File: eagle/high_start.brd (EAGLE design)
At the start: 100.8 x 80.8 mm, 32 parts, among them Q1 16Mhz, Q2 IRF510, Q3 IRF510, Q4 IRF510, U2 ATMEGA328P_PDIP, X1 22-23-2041, X2 22-23-2041, X3 22-23-2041, X4 22-23-2041

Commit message: tied led cathodes to gnd
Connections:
- net GND: now also LED1.K, LED2.K, LED3.K
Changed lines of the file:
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@@
 <contactref element="IGN3" pad="1"/>
 <contactref element="IGN2" pad="1"/>
+<contactref element="LED1" pad="K"/>
+<contactref element="LED3" pad="K"/>
+<contactref element="LED2" pad="K"/>
 <wire x1="-68.58" y1="-190.5" x2="-68.58" y2="-175.26" width="0" layer="19" extent="1-1"/>
 <wire x1="-68.58" y1="-205.74" x2="-68.58" y2="-190.5" width="0" layer="19" extent="1-1"/>
@@
 <wire x1="-73.66" y1="-279.4" x2="-73.66" y2="-264.16" width="0" layer="19" extent="1-1"/>
 <wire x1="-73.66" y1="-294.64" x2="-73.66" y2="-279.4" width="0" layer="19" extent="1-1"/>
+<wire x1="-72.39" y1="-309.88" x2="-73.66" y2="-294.64" width="0" layer="19" extent="1-1"/>
+<wire x1="-72.39" y1="-323.85" x2="-72.39" y2="-309.88" width="0" layer="19" extent="1-1"/>
+<wire x1="-72.39" y1="-337.82" x2="-72.39" y2="-323.85" width="0" layer="19" extent="1-1"/>
 <wire x1="-24.13" y1="-86.36" x2="-68.58" y2="-175.26" width="0" layer="19" extent="1-1"/>
 <wire x1="-24.13" y1="-71.12" x2="-24.13" y2="-86.36" width="0" layer="19" extent="1-1"/>

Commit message: added battery and reg and layed out board
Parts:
- removed GPS_SPI: 22-23-2021, con-molex:22-23-2021
- removed X1, X2, X3, X4: 22-23-2041, con-molex:22-23-2041
- added BATTERY: 22-23-2021, con-molex:22-23-2021
- added C4: 22u, rcl:B45181A
- added GPS, I2C_1, I2C_2, I2C_3: 22-23-2041, con-molex:22-23-2041
- added IC1: 7805L, linear:TO92
- moved LED3 408.3 mm to (91.4, 35.6), turned to 270 degrees
- moved LED2 384.0 mm to (91.4, 22.9), turned to 270 degrees
- moved IGN3 362.9 mm to (91.4, 29.2), turned to 270 degrees
- moved LED1 360.1 mm to (91.4, 10.2), turned to 270 degrees
- moved IGN2 338.2 mm to (91.4, 16.5), turned to 270 degrees
- moved R4 322.9 mm to (86.4, 33.0), turned to 270 degrees
- moved IGN1 314.1 mm to (91.4, 3.81), turned to 270 degrees
- moved R3 299.9 mm to (86.4, 20.3), turned to 270 degrees
- moved R2 277.6 mm to (86.4, 7.62), turned to 270 degrees
- moved SERVO3 245.5 mm to (54.6, 5.08), turned to 180 degrees
- moved SERVO2 237.9 mm to (54.6, 11.4), turned to 180 degrees
- moved Q4 222.0 mm to (69.8, 33.0), turned to 270 degrees
- moved D3 220.9 mm to (26.7, 38.1), turned to 270 degrees
- moved SERVO1 210.8 mm to (19.1, 15.2), turned to 270 degrees
- moved D2 183.5 mm to (29.2, 38.1), turned to 270 degrees
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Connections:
- net +5V: now also C4.+, GPS.4, I2C_1.4, I2C_2.4, I2C_3.4, IC1.1; no longer X1.4, X2.4, X3.4, X4.4
- net +9V: now also BATTERY.2, IC1.3
- net GND: now also BATTERY.1, C4.-, GPS.3, I2C_1.3, I2C_2.3, I2C_3.3, IC1.2; no longer X1.3, X2.3, X3.3, X4.3
- net N$1: now also I2C_1.2, I2C_2.2, I2C_3.2; no longer X1.2, X2.2, X3.2, X4.2
- net N$2: now also I2C_1.1, I2C_2.1, I2C_3.1; no longer X1.1, X2.1, X3.1, X4.1
- net N$3: now also GPS.1; no longer GPS_SPI.2
- net N$6: now also GPS.2; no longer GPS_SPI.1
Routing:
- net GND: track 123.6 -> 0.00 mm
- net +5V: track 33.9 -> 0.00 mm
- net N$5: track 15.2 -> 0.00 mm
- net N$43: track 14.6 -> 0.00 mm
- net N$4: track 14.3 -> 0.00 mm
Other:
- board size 100.8 x 80.8 mm -> 100.1 x 80 mm

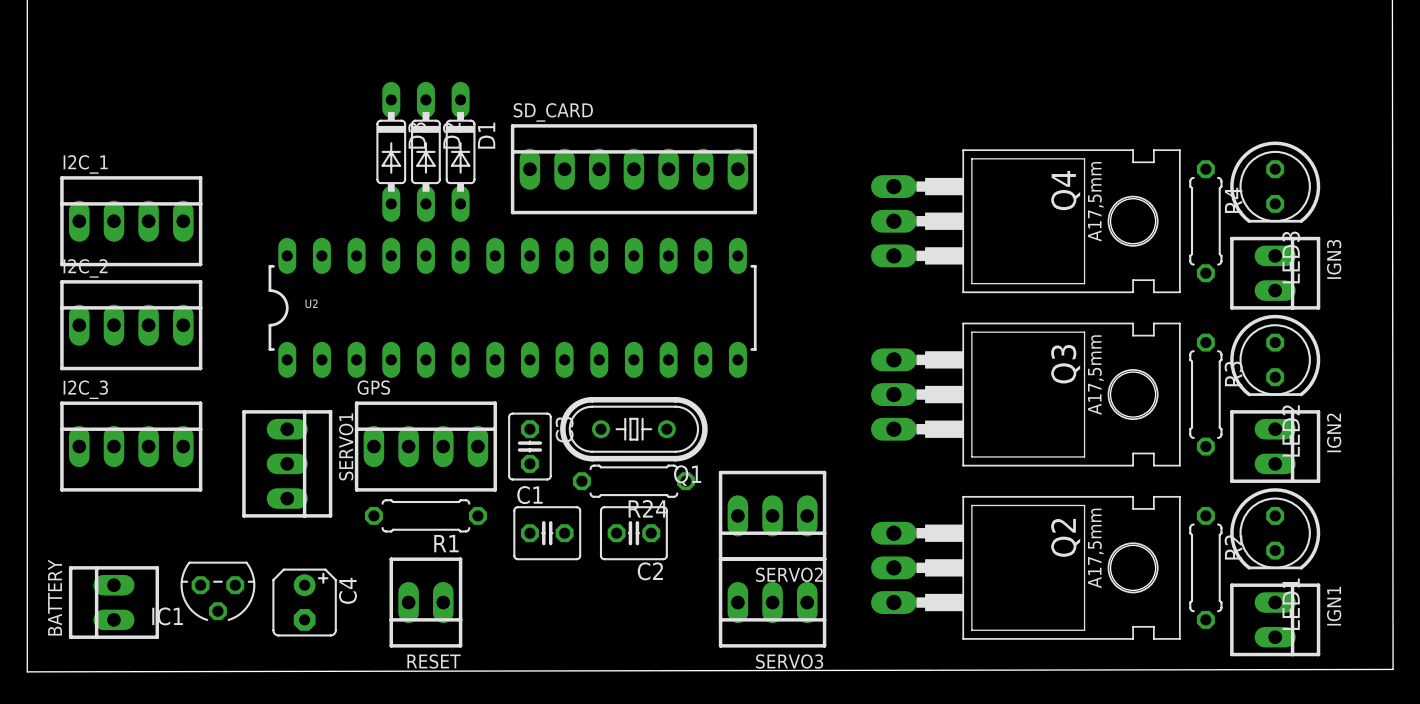
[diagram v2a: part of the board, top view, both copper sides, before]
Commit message: moved power connector between fets and micro
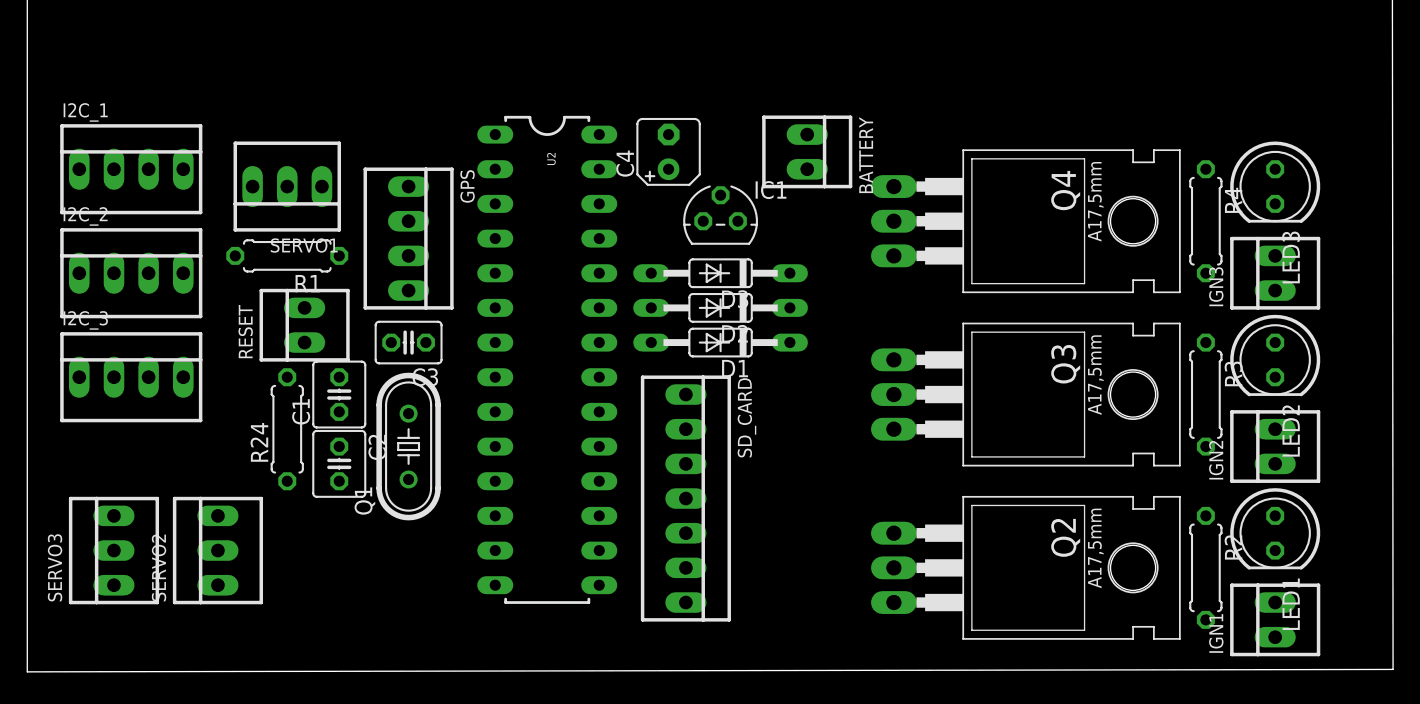
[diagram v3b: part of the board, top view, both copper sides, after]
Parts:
- D1, D2, D3: value 1N4148DO35-7 -> 1N4148DO35-10; device diode:DO35-7 -> diode:DO35-10
- moved BATTERY 60.6 mm to (57.1, 38.1), turned to 270 degrees
- moved SERVO3 48.4 mm to (6.35, 8.89), turned to 90 degrees
- moved IC1 45.5 mm to (50.8, 33.0), turned to 0 degrees
- moved C4 42.4 mm to (47.0, 38.1), turned to 90 degrees
- moved SERVO2 40.7 mm to (14.0, 8.89), turned to 90 degrees
- moved D3 25.7 mm to (50.8, 29.2), turned to 180 degrees
- moved R24 25.7 mm to (19.1, 17.8), turned to 90 degrees
- moved SD_CARD 24.4 mm to (48.3, 12.7), turned to 270 degrees
- moved D2 24.4 mm to (50.8, 26.7), turned to 180 degrees
- moved D1 23.6 mm to (50.8, 24.1), turned to 180 degrees
- moved C2 22.2 mm to (22.9, 15.2), turned to 270 degrees
- moved RESET 22.2 mm to (20.3, 25.4), turned to 90 degrees
- moved R1 21.6 mm to (19.1, 30.5)
- moved SERVO1 20.3 mm to (19.1, 35.6), turned to 180 degrees
- moved C1 18.3 mm to (22.9, 20.3), turned to 90 degrees
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
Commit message: routed
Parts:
- moved SERVO1 21.6 mm to (8.89, 16.5)
- moved I2C_3 5.08 mm to (7.62, 26.7), turned to 180 degrees
- moved I2C_2 3.81 mm to (7.62, 33.0), turned to 180 degrees
- moved R1 3.30 mm to (22.4, 30.5), turned to 90 degrees
- moved I2C_1 2.54 mm to (7.62, 39.4), turned to 180 degrees
- moved RESET 2.54 mm to (17.8, 25.4), turned to 180 degrees
- moved SD_CARD 1.27 mm to (49.5, 12.7)
- moved C4 0.51 mm to (47.5, 38.1)
- turned LED1 to 0 degrees
- turned LED2 to 0 degrees
- turned LED3 to 0 degrees
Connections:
- net +5V: now also U2.21
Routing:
- net GND: track 0.00 -> 254.5 mm, vias 0 -> 4
- net +5V: track 0.00 -> 184.5 mm, vias 0 -> 2
- net +9V: track 0.00 -> 65.2 mm
- net N$15: track 0.00 -> 53.9 mm
- net N$1: track 0.00 -> 49.9 mm
- net N$2: track 0.00 -> 47.8 mm
- net N$7: track 0.00 -> 40.3 mm
- net N$8: track 0.00 -> 34.8 mm
- net N$17: track 0.00 -> 31.6 mm
- net N$24: track 0.00 -> 28.8 mm
- net N$25: track 0.00 -> 28.8 mm
- net N$26: track 0.00 -> 28.2 mm
- net N$43: track 0.00 -> 25.5 mm
- net N$16: track 0.00 -> 23.5 mm
- net N$4: track 0.00 -> 16.7 mm
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
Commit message: milling on board
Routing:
- net N$24: track 28.8 -> 30.4 mm
- net N$17: track 31.6 -> 32.6 mm
- net N$16: track 23.5 -> 24.4 mm
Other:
- board size 100.1 x 80 mm -> 100.1 x 80.8 mm
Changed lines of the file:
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@@
 <wire x1="100" y1="80" x2="0" y2="80" width="0" layer="20"/>
 <wire x1="0" y1="80" x2="0" y2="0" width="0" layer="20"/>
+<wire x1="15.748" y1="39.37" x2="17.526" y2="39.37" width="1.6764" layer="46"/>
+<wire x1="17.526" y1="39.37" x2="17.526" y2="37.592" width="1.6764" layer="46"/>
+<wire x1="17.526" y1="37.592" x2="15.748" y2="37.592" width="1.6764" layer="46"/>
+<wire x1="15.748" y1="37.592" x2="15.748" y2="39.37" width="1.6764" layer="46"/>
+<wire x1="21.844" y1="6.35" x2="29.972" y2="6.35" width="1.6764" layer="46"/>
+<wire x1="29.972" y1="6.35" x2="29.972" y2="4.572" width="1.6764" layer="46"/>
+<wire x1="29.972" y1="4.572" x2="21.844" y2="4.572" width="1.6764" layer="46"/>
+<wire x1="21.844" y1="4.572" x2="21.844" y2="6.35" width="1.6764" layer="46"/>
+<wire x1="69.342" y1="35.052" x2="83.312" y2="35.052" width="1.6764" layer="46"/>
+<wire x1="83.312" y1="35.052" x2="83.312" y2="33.274" width="1.6764" layer="46"/>
+<wire x1="83.312" y1="33.274" x2="69.342" y2="33.274" width="1.6764" layer="46"/>
+<wire x1="69.342" y1="33.274" x2="69.342" y2="35.052" width="1.6764" layer="46"/>
+<wire x1="69.342" y1="8.382" x2="83.312" y2="8.382" width="1.6764" layer="46"/>
+<wire x1="83.312" y1="8.382" x2="83.312" y2="6.604" width="1.6764" layer="46"/>
+<wire x1="83.312" y1="6.604" x2="69.342" y2="6.604" width="1.6764" layer="46"/>
+<wire x1="69.342" y1="6.604" x2="69.342" y2="8.382" width="1.6764" layer="46"/>
+<wire x1="1.27" y1="44.45" x2="1.27" y2="0.508" width="1.6764" layer="46"/>
+<wire x1="1.27" y1="0.508" x2="2.54" y2="-0.762" width="1.6764" layer="46"/>
+<wire x1="2.54" y1="-0.762" x2="93.98" y2="-0.762" width="1.6764" layer="46"/>
+<wire x1="93.98" y1="-0.762" x2="96.266" y2="1.778" width="1.6764" layer="46"/>
+<wire x1="96.266" y1="1.778" x2="96.266" y2="39.37" width="1.6764" layer="46"/>
+<wire x1="96.266" y1="39.37" x2="92.202" y2="41.91" width="1.6764" layer="46"/>
+<wire x1="92.202" y1="41.91" x2="43.18" y2="41.91" width="1.6764" layer="46"/>
+<wire x1="43.18" y1="41.91" x2="38.354" y2="45.72" width="1.6764" layer="46"/>
+<wire x1="38.354" y1="45.72" x2="2.54" y2="45.72" width="1.6764" layer="46"/>
+<wire x1="1.27" y1="44.45" x2="2.54" y2="45.72" width="1.6764" layer="46"/>
+<wire x1="69.342" y1="27.686" x2="69.342" y2="20.32" width="1.6764" layer="46"/>
+<wire x1="69.342" y1="20.32" x2="83.312" y2="20.32" width="1.6764" layer="46"/>
+<wire x1="83.312" y1="20.32" x2="83.312" y2="27.686" width="1.6764" layer="46"/>
+<wire x1="83.312" y1="27.686" x2="69.342" y2="27.686" width="1.6764" layer="46"/>
 </plain>
 <attributes>
@@
 <contactref element="SERVO2" pad="1"/>
 <wire x1="31.0642" y1="13.4366" x2="33.8836" y2="13.4366" width="0.7112" layer="16"/>
-<wire x1="24.0538" y1="6.4262" x2="31.0642" y2="13.4366" width="0.7112" layer="16"/>
-<wire x1="14.0208" y1="6.4262" x2="24.0538" y2="6.4262" width="0.7112" layer="16"/>
+<wire x1="15.9258" y1="6.4262" x2="17.78" y2="10.16" width="0.7112" layer="16"/>
+<wire x1="17.78" y1="10.16" x2="19.05" y2="11.43" width="0.7112" layer="16"/>
+<wire x1="19.05" y1="11.43" x2="29.21" y2="11.43" width="0.7112" layer="16"/>
+<wire x1="29.21" y1="11.43" x2="31.0642" y2="13.2842" width="0.7112" layer="16"/>
+<wire x1="31.0642" y1="13.2842" x2="31.0642" y2="13.4366" width="0.7112" layer="16"/>
+<wire x1="14.0208" y1="6.4262" x2="15.9258" y2="6.4262" width="0.7112" layer="16"/>
 <wire x1="33.8836" y1="13.4366" x2="34.29" y2="13.97" width="0.7112" layer="16"/>
 <wire x1="14.0208" y1="6.4262" x2="13.97" y2="6.35" width="0.7112" layer="16"/>
@@
 <contactref element="SERVO3" pad="1"/>
 <contactref element="U2" pad="12"/>
-<wire x1="31.242" y1="11.0998" x2="33.8836" y2="11.0998" width="0.7112" layer="16"/>
-<wire x1="24.8158" y1="4.6736" x2="31.242" y2="11.0998" width="0.7112" layer="16"/>
-<wire x1="7.5946" y1="4.6736" x2="24.8158" y2="4.6736" width="0.7112" layer="16"/>
+<wire x1="31.496" y1="11.0998" x2="33.8836" y2="11.0998" width="0.7112" layer="16"/>
+<wire x1="17.1958" y1="4.6736" x2="19.812" y2="9.906" width="0.7112" layer="16"/>
+<wire x1="19.812" y1="9.906" x2="29.718" y2="9.906" width="0.7112" layer="16"/>
+<wire x1="29.718" y1="9.906" x2="31.242" y2="10.922" width="0.7112" layer="16"/>
+<wire x1="31.242" y1="10.922" x2="31.496" y2="11.0998" width="0.7112" layer="16"/>
+<wire x1="7.5946" y1="4.6736" x2="17.1958" y2="4.6736" width="0.7112" layer="16"/>
 <wire x1="6.4262" y1="5.842" x2="7.5946" y2="4.6736" width="0.7112" layer="16"/>
 <wire x1="33.8836" y1="11.0998" x2="34.29" y2="11.43" width="0.7112" layer="16"/>
@@
 <contactref element="R2" pad="1"/>
 <contactref element="LED1" pad="A"/>
-<wire x1="87.3252" y1="11.684" x2="86.4616" y2="11.684" width="0.7112" layer="16"/>
+<wire x1="86.8172" y1="11.43" x2="86.4616" y2="11.684" width="0.7112" layer="16"/>
 <wire x1="86.4616" y1="11.684" x2="86.36" y2="11.43" width="0.7112" layer="16"/>
-<wire x1="87.3252" y1="11.684" x2="90.17" y2="10.16" width="0.7112" layer="16"/>
+<wire x1="86.8172" y1="11.43" x2="90.17" y2="10.16" width="0.7112" layer="16"/>
 </signal>
 <signal name="N$22">
 <contactref element="R3" pad="1"/>
 <contactref element="LED2" pad="A"/>
-<wire x1="87.3252" y1="24.5364" x2="86.4616" y2="24.5364" width="0.7112" layer="16"/>
-<wire x1="86.4616" y1="24.5364" x2="86.36" y2="24.13" width="0.7112" layer="16"/>
-<wire x1="87.3252" y1="24.5364" x2="90.17" y2="22.86" width="0.7112" layer="16"/>
+<wire x1="87.3252" y1="23.7744" x2="86.4616" y2="23.7744" width="0.7112" layer="16"/>
+<wire x1="86.4616" y1="23.7744" x2="86.36" y2="24.13" width="0.7112" layer="16"/>
+<wire x1="87.3252" y1="23.7744" x2="90.17" y2="22.86" width="0.7112" layer="16"/>
 </signal>
 <signal name="N$23">
@@
 <wire x1="86.4616" y1="4.0894" x2="86.36" y2="3.81" width="0.7112" layer="16"/>
 <wire x1="91.1352" y1="5.2578" x2="91.44" y2="5.08" width="0.7112" layer="16"/>
-<wire x1="77.1144" y1="4.6736" x2="63.6778" y2="4.6736" width="1.016" layer="16"/>
-<wire x1="85.217" y1="4.191" x2="77.1144" y2="4.6736" width="1.016" layer="16"/>
-<wire x1="85.2932" y1="4.191" x2="85.217" y2="4.191" width="1.016" layer="16"/>
-<wire x1="86.3854" y1="3.7592" x2="85.2932" y2="4.191" width="1.016" layer="16"/>
+<wire x1="63.3984" y1="4.6736" x2="63.6778" y2="4.6736" width="1.016" layer="16"/>
+<wire x1="68.199" y1="2.413" x2="63.3984" y2="4.6736" width="1.016" layer="16"/>
+<wire x1="85.2932" y1="2.413" x2="68.199" y2="2.413" width="1.016" layer="16"/>
+<wire x1="86.3854" y1="3.7592" x2="85.2932" y2="2.413" width="1.016" layer="16"/>
 <wire x1="63.6778" y1="4.6736" x2="63.5" y2="5.08" width="0.7112" layer="16"/>
 <wire x1="86.3854" y1="3.7592" x2="86.36" y2="3.81" width="0.7112" layer="16"/>
@@
 <wire x1="86.4616" y1="16.9418" x2="86.36" y2="16.51" width="0.7112" layer="16"/>
 <wire x1="91.1352" y1="17.526" x2="91.44" y2="17.78" width="0.7112" layer="16"/>
-<wire x1="77.1144" y1="17.526" x2="63.6778" y2="17.526" width="1.016" layer="16"/>
-<wire x1="85.217" y1="17.0434" x2="77.1144" y2="17.526" width="1.016" layer="16"/>
+<wire x1="83.4644" y1="17.526" x2="63.6778" y2="17.526" width="1.016" layer="16"/>
+<wire x1="85.217" y1="17.0434" x2="83.4644" y2="17.526" width="1.016" layer="16"/>
 <wire x1="85.2932" y1="17.0434" x2="85.217" y2="17.0434" width="1.016" layer="16"/>
 <wire x1="86.3854" y1="16.6116" x2="85.2932" y2="17.0434" width="1.016" layer="16"/>
@@
 <wire x1="90.6272" y1="30.2006" x2="86.8426" y2="29.21" width="1.016" layer="16"/>
 <wire x1="90.6272" y1="30.2006" x2="91.44" y2="30.48" width="1.016" layer="16"/>
-<wire x1="77.1144" y1="30.3784" x2="63.6778" y2="30.3784" width="1.016" layer="16"/>
-<wire x1="84.5312" y1="29.3116" x2="77.1144" y2="30.3784" width="1.016" layer="16"/>
-<wire x1="84.709" y1="29.3116" x2="84.5312" y2="29.3116" width="1.016" layer="16"/>
-<wire x1="85.8774" y1="29.21" x2="84.709" y2="29.3116" width="1.016" layer="16"/>
+<wire x1="83.4644" y1="30.3784" x2="63.6778" y2="30.3784" width="1.016" layer="16"/>
+<wire x1="85.8012" y1="29.3116" x2="83.4644" y2="30.3784" width="1.016" layer="16"/>
+<wire x1="85.979" y1="29.3116" x2="85.8012" y2="29.3116" width="1.016" layer="16"/>
+<wire x1="85.8774" y1="29.21" x2="85.979" y2="29.3116" width="1.016" layer="16"/>
 <wire x1="63.6778" y1="30.3784" x2="63.5" y2="30.48" width="0.7112" layer="16"/>
 <wire x1="85.8774" y1="29.21" x2="86.36" y2="29.21" width="1.016" layer="16"/>
